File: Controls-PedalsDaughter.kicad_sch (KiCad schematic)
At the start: 12 parts, among them J2 Conn_02x03_Counter_Clockwise

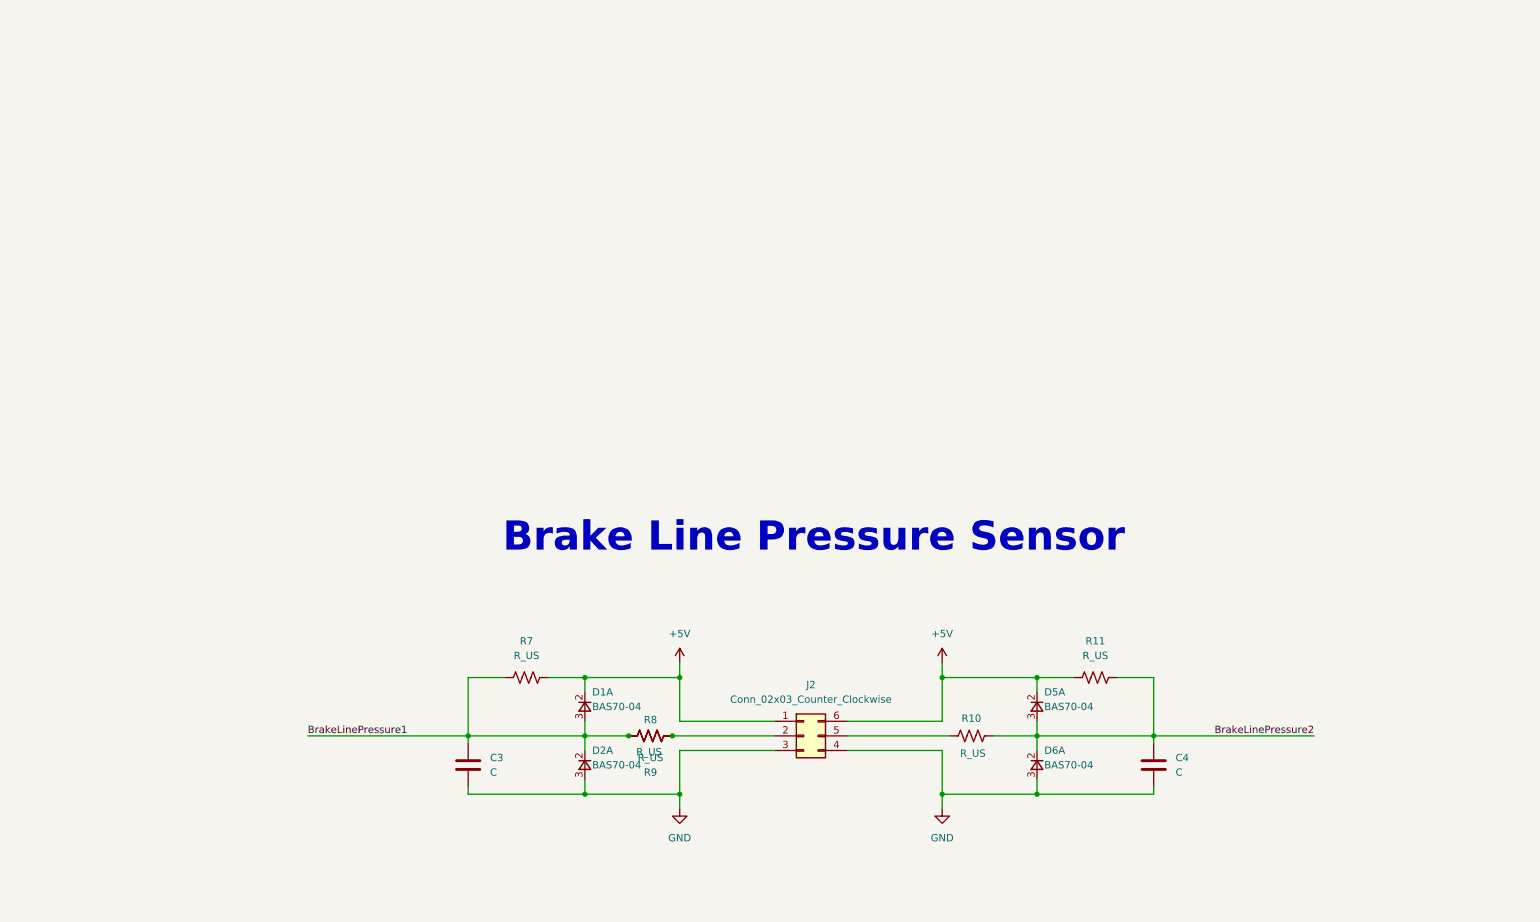
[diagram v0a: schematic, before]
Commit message: Started Pedalboard Brakeline Fluid Sensor
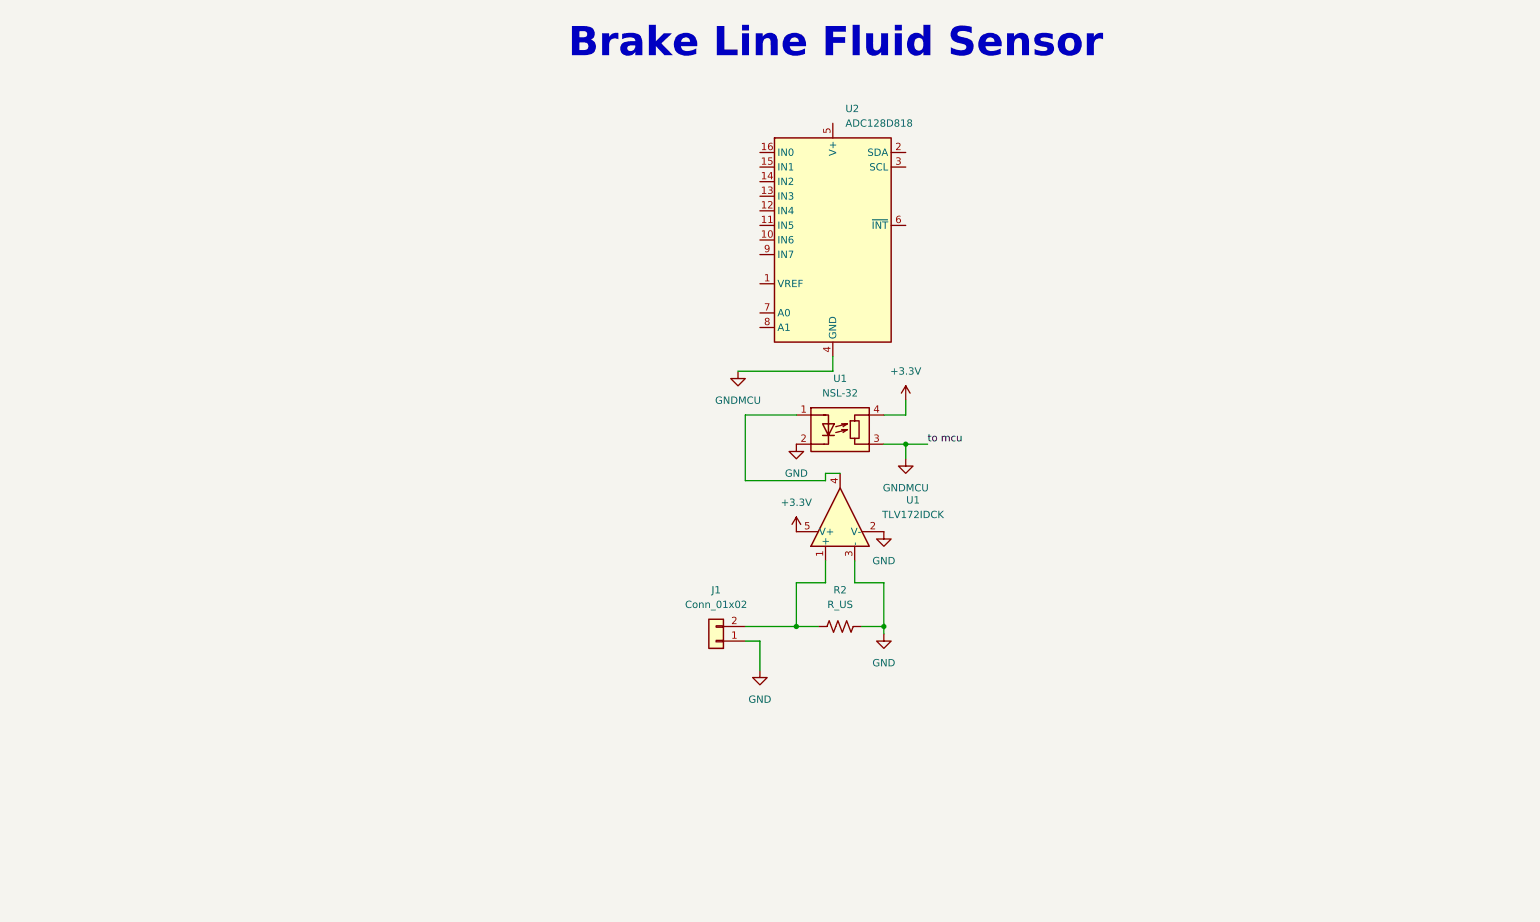
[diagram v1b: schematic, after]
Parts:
- removed C3, C4: C, symbol Device:C
- removed D1, D2, D5, D6: BAS70-04, Package_TO_SOT_SMD:SOT-23, symbol Dashboard-rescue:BAS70-04-utsvt-chips
- removed J2: Conn_02x03_Counter_Clockwise, symbol Connector_Generic:Conn_02x03_Counter_Clockwise
- removed R10, R11, R7, R8, R9: R_US, symbol Device:R_US
- added J1: Conn_01x02, symbol Connector_Generic:Conn_01x02
- added R2: R_US, symbol Device:R_US
- added U1: TLV172IDCK, Package_TO_SOT_SMD:SOT-353_SC-70-5, symbol Amplifier_Operational:TLV172IDCK
- added U1: NSL-32, OptoDevice:Luna_NSL-32, symbol Isolator:NSL-32
- added U2: ADC128D818, Package_SO:TSSOP-16_4.4x5mm_P0.65mm, symbol Analog_ADC:ADC128D818
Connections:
- net GND: now also J1.1 (Pin_1), R2.1, U1.2 (K), U1.2 (V-), U1.3 (-)
- new net: J1.2 (Pin_2), R2.2, U1.1 (+)
- new net: U1.1 (A), U1.4
- new net +3.3V: U1.4 (R), U1.5 (V+)
- new net GNDMCU: U1.3 (R), U2.4 (GND)
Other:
- note added: "Brake Line Fluid Sensor"
- note removed: "Brake Line Pressure Sensor"

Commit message: Added  resister values
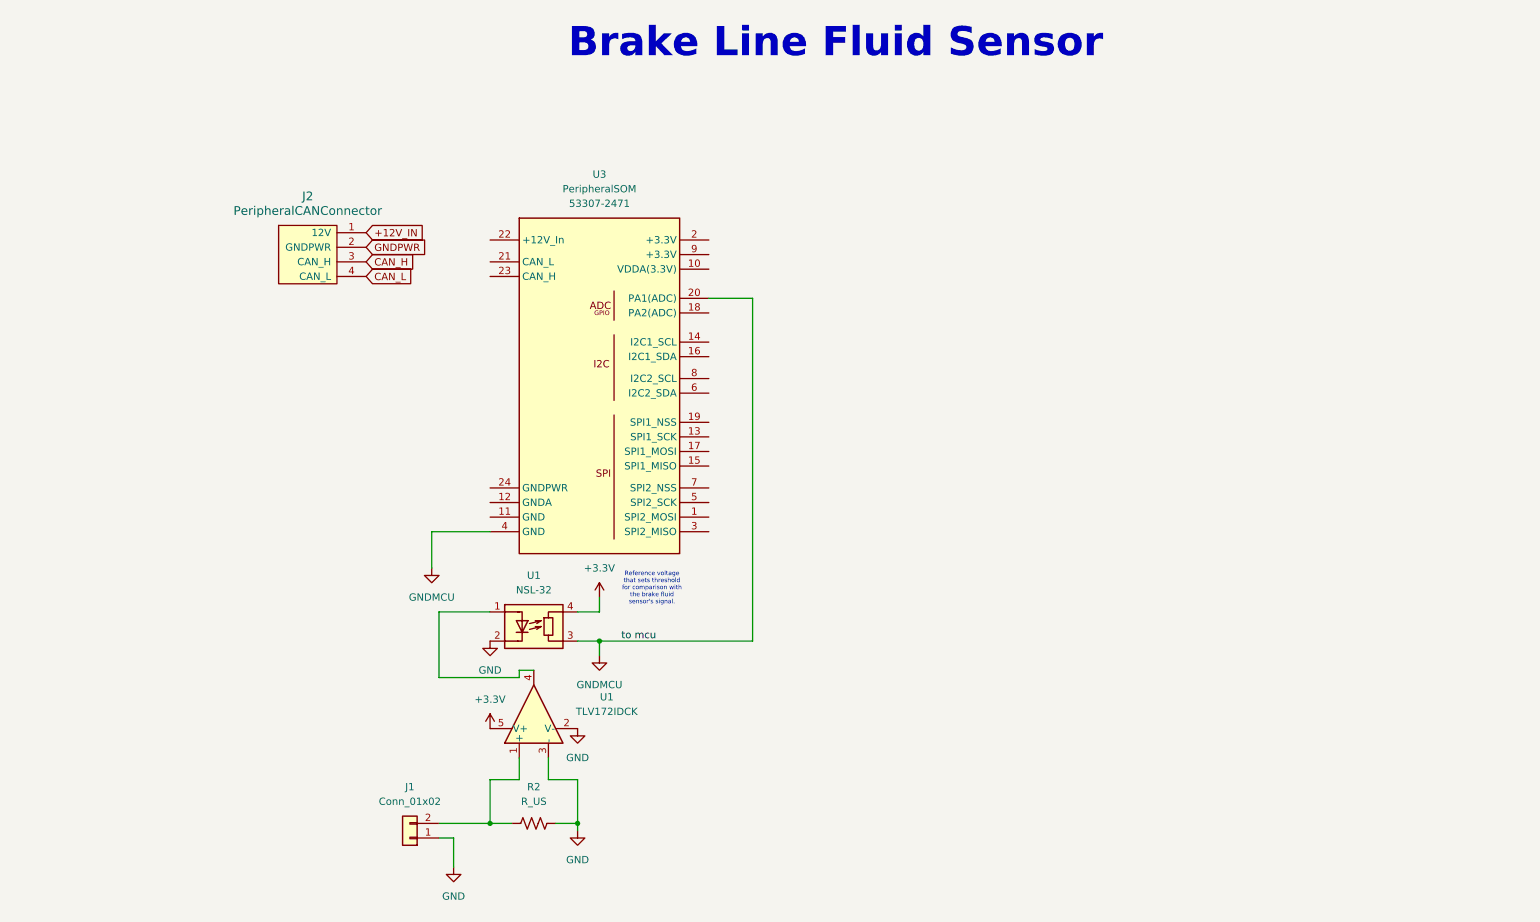
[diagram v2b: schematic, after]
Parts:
- removed U2: ADC128D818, Package_SO:TSSOP-16_4.4x5mm_P0.65mm, symbol Analog_ADC:ADC128D818
- added J2: PeripheralCANConnector, UTSVT_Connectors:Molex_MicroFit3.0_1x4xP3.00mm_PolarizingPeg_Vertical, symbol utsvt-connectors:PeripheralCANConnector
- added U3: PeripheralSOM, UTSVT_Special:PeripheralSOM, symbol utsvt-misc:PeripheralSOM
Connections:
- net GNDMCU: now also U3.20 (PA1(ADC)), U3.4 (GND)
- new net +12V_IN: J2.1 (12V)
- new net CAN_H: J2.3 (CAN_H)
- new net CAN_L: J2.4 (CAN_L)
- new net GNDPWR: J2.2 (GNDPWR)
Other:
- note added: "Reference voltage that sets threshold for comparison with the brake fluid sensor's signal."
- moved on the sheet: J1, R2, U1

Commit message: Deleted Starter Project File. Should be able to open now.
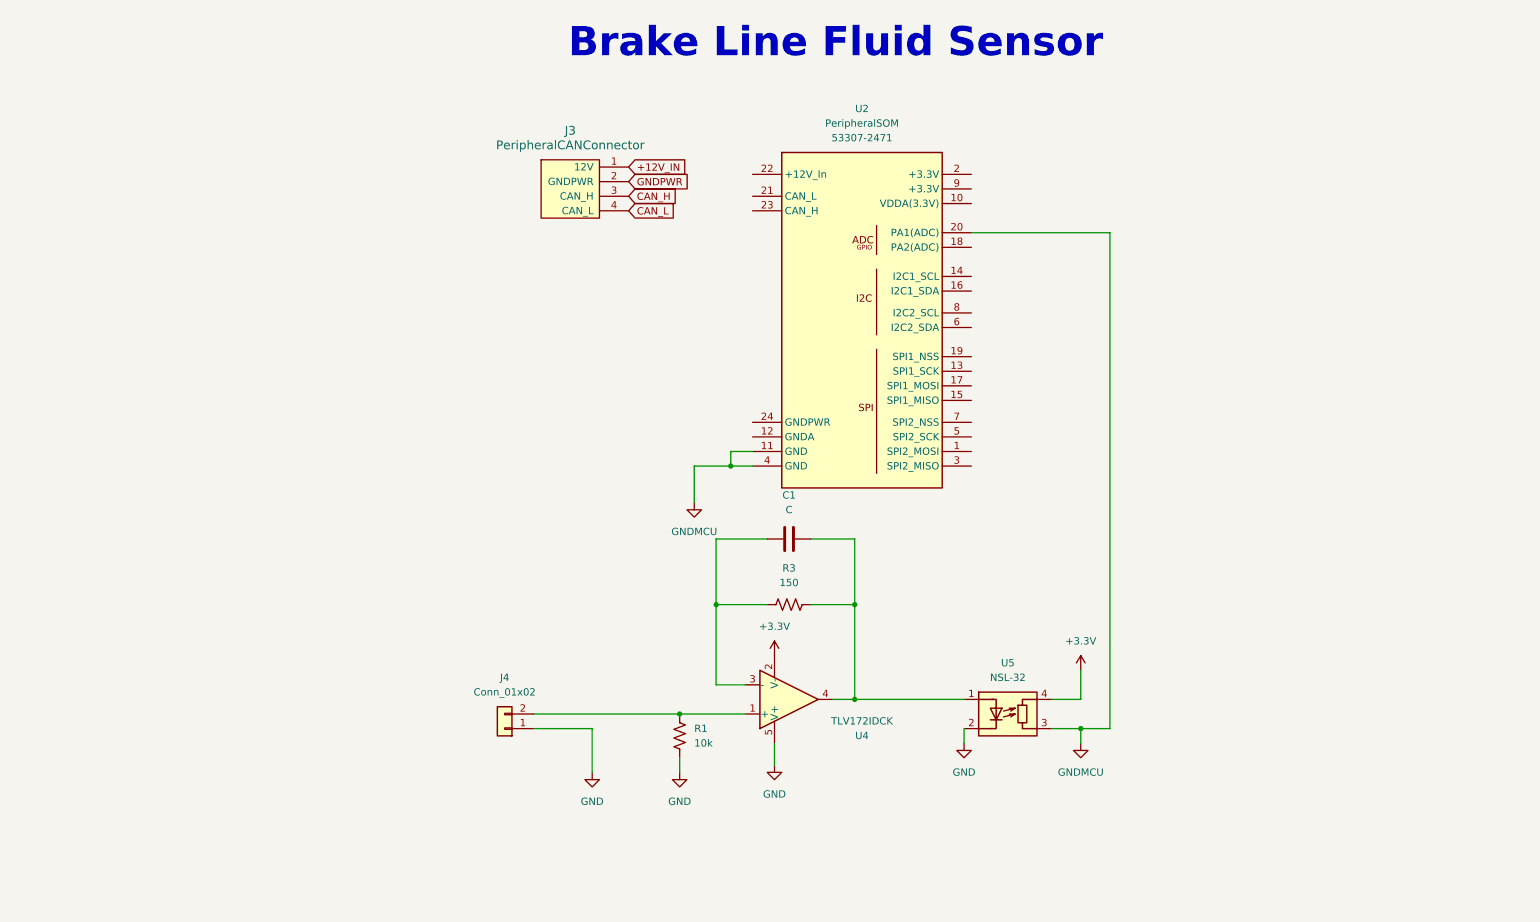
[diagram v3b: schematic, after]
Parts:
- removed J1: Conn_01x02, symbol Connector_Generic:Conn_01x02
- removed J2: PeripheralCANConnector, UTSVT_Connectors:Molex_MicroFit3.0_1x4xP3.00mm_PolarizingPeg_Vertical, symbol utsvt-connectors:PeripheralCANConnector
- removed R2: R_US, symbol Device:R_US
- removed U1: TLV172IDCK, Package_TO_SOT_SMD:SOT-353_SC-70-5, symbol Amplifier_Operational:TLV172IDCK
- removed U1: NSL-32, OptoDevice:Luna_NSL-32, symbol Isolator:NSL-32
- removed U3: PeripheralSOM, UTSVT_Special:PeripheralSOM, symbol utsvt-misc:PeripheralSOM
- added C1: C, symbol Device:C
- added J3: PeripheralCANConnector, UTSVT_Connectors:Molex_MicroFit3.0_1x4xP3.00mm_PolarizingPeg_Vertical, symbol utsvt-connectors:PeripheralCANConnector
- added J4: Conn_01x02, symbol Connector_Generic:Conn_01x02
- added R1: 10k, symbol Device:R_US
- added R3: 150, symbol Device:R_US
- added U2: PeripheralSOM, UTSVT_Special:PeripheralSOM, symbol utsvt-misc:PeripheralSOM
- added U4: TLV172IDCK, Package_TO_SOT_SMD:SOT-353_SC-70-5, symbol Amplifier_Operational:TLV172IDCK
- added U5: NSL-32, OptoDevice:Luna_NSL-32, symbol Isolator:NSL-32
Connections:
- net +12V_IN: now also J3.1 (12V)
- net +3.3V: now also U4.2 (V-), U5.4 (R)
- net CAN_H: now also J3.3 (CAN_H)
- net CAN_L: now also J3.4 (CAN_L)
- net GND: now also J4.1 (Pin_1), R1.2, U4.5 (V+), U5.2 (K)
- net GNDMCU: now also U2.11 (GND), U2.20 (PA1(ADC)), U2.4 (GND), U5.3 (R)
- net GNDPWR: now also J3.2 (GNDPWR)
- new net: J4.2 (Pin_2), R1.1, U4.1 (+)
- new net: C1.1, R3.1, U4.3 (-)
- new net: C1.2, R3.2, U4.4, U5.1 (A)
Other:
- note removed: "Reference voltage that sets threshold for comparison with the brake fluid sensor's signal."

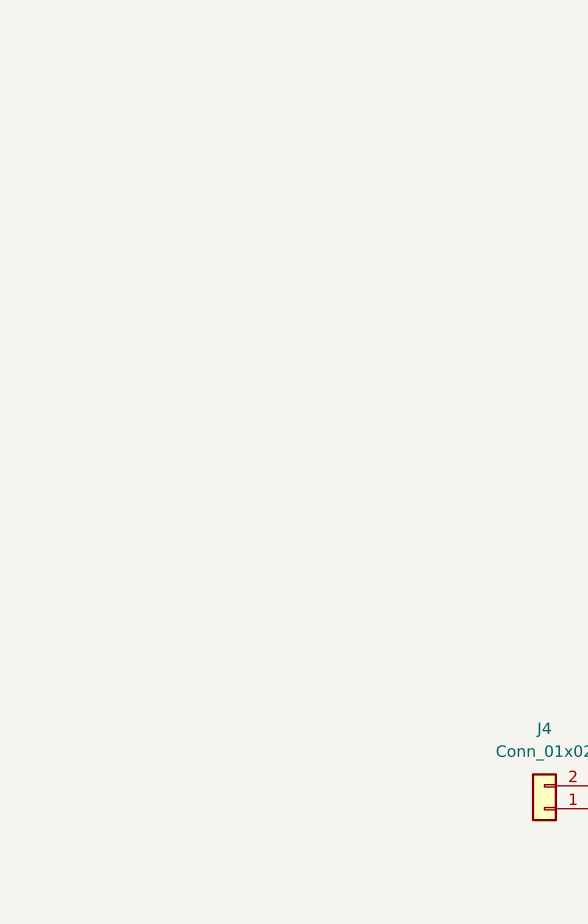
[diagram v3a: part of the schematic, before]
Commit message: Added pedals
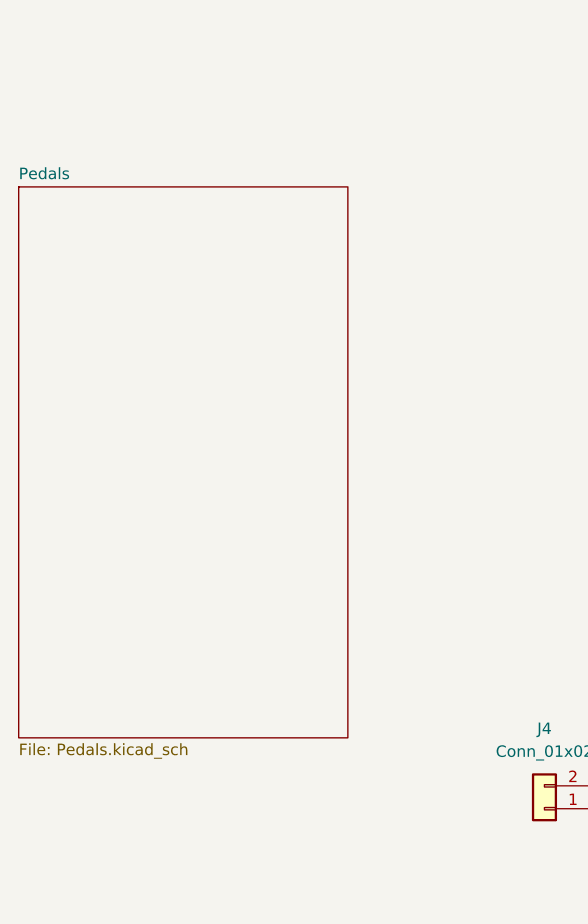
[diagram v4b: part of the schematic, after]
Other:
- added sheet Pedals (Pedals.kicad_sch)
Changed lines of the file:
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@@
+		)
+	)
+	(sheet
+		(at 33.02 73.152)
+		(size 36.576 61.214)
+		(fields_autoplaced yes)
+		(stroke
+			(width 0.1524)
+			(type solid)
+		)
+		(fill
+			(color 0 0 0 0.0000)
+		)
+		(property "Sheetname" "Pedals"
+			(at 33.02 72.4404 0)
+			(effects
+				(font
+					(size 1.27 1.27)
+				)
+				(justify left bottom)
+			)
+		)
+		(property "Sheetfile" "Pedals.kicad_sch"
+			(at 33.02 134.9506 0)
+			(effects
+				(font
+					(size 1.27 1.27)
+				)
+				(justify left top)
+			)
+		)
+		(instances
+			(project "Controls-PedalsDaughter"
+				(path "/30d77876-714b-4f1b-9bad-b74eb43ddcf6"
+					(page "2")
+				)
+			)
 		)
 	)

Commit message: Combined
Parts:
- added C2: 10u, UTSVT_Passive:C_2220_5750Metric, symbol Device:C
- added C3: C, symbol Device:C
- added D1: TVS, Diode_SMD:D_SOD-323, symbol Device:D
- added D2, D3: D, symbol Device:D
- added J1: PowerConn, UTSVT_Connectors:Molex_MicroFit3.0_1x2xP3.00mm_PolarizingPeg_Vertical, symbol Connector_Generic:Conn_01x02
- added J2: Accel Pos. Sensor, symbol Connector_Generic:Conn_02x03_Top_Bottom
- added R2: 8.2k, symbol Device:R_US
- added R4: 22k, symbol Device:R_US
- added TP1: +12V_TP, TestPoint:TestPoint_Pad_1.5x1.5mm, symbol Connector:TestPoint
- added TP2: GNDPWR_TP, TestPoint:TestPoint_Pad_1.5x1.5mm, symbol Connector:TestPoint
- added TP3: +5V_TP, TestPoint:TestPoint_Pad_1.5x1.5mm, symbol Connector:TestPoint
- added TP4: GND_TP, TestPoint:TestPoint_Pad_1.5x1.5mm, symbol Connector:TestPoint
- added U1: RI3-1205S, UTSVT_ICs:RI3_DC_Converter, symbol Dashboard-rescue:RI3-1205S-utsvt-power-regulators
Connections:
- net +12V_IN is gone; now on net +12V: J3.1 (12V)
- net GNDPWR is gone; now on net GND: J3.2 (GNDPWR)
- net +3.3V: now also U2.10 (VDDA(3.3V)), U2.2 (+3.3V), U2.9 (+3.3V), D2.2 (A)
- net CAN_H: now also U2.23 (CAN_H)
- net CAN_L: now also U2.21 (CAN_L)
- net GND: now also U2.24 (GNDPWR), C2.2, D1.2 (A), J1.2 (Pin_2), TP2.1, U1.1 (-Vin)
- net GNDMCU: now also C3.1, D3.2 (A), J2.1 (Pin_1), J2.3 (Pin_3), R4.2, TP4.1, U1.3 (-Vout)
- net Accel: now reaches U2.18 (PA2(ADC))
- net Accel: now also C3.2, D2.1 (K), D3.1 (K), R2.1, R4.1
- net +12V: now reaches U2.22 (+12V_In)
- net +12V: now also C2.1, D1.1 (K), J1.1 (Pin_1), TP1.1, U1.2 (+Vin)
- new net: J2.5 (Pin_5), R2.2
- new net +5V: J2.4 (Pin_4), J2.6 (Pin_6), TP3.1, U1.4 (+Vout)
- no-connect marks 0 -> 14
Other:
- removed sheet Pedals
- note added: "0.5V - 4.5V Analog signal"
- note added: "4.5V -> 3.278V"
- note added: "Based on: https://www.akao.co.uk/manuals/Link%20G4+%20Manual/nissan_vq35.htm"
- note added: "ISOLATED PWR"
- note added: "Local (Leader Board) GND (Internal)"
- note added: "Notes: · Motor + refers to the pin that has battery voltage applied to it to open the throttle. · It is recommended to use shielded cables for TPS and APS sensors. · To prevent back feeding, the throttle motor relay must be controlled from a non flywheeled output such as a spare Ignition or Injection channel. - If the sensor and microcontroller are powered from different systems or are physically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"
- note added: "Power GND (External)"
- note added: "Redundant Signal"
- moved on the sheet: C1, J3, J4, R1, R3, U2, U4, U5
